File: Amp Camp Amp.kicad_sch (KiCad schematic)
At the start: 0 parts

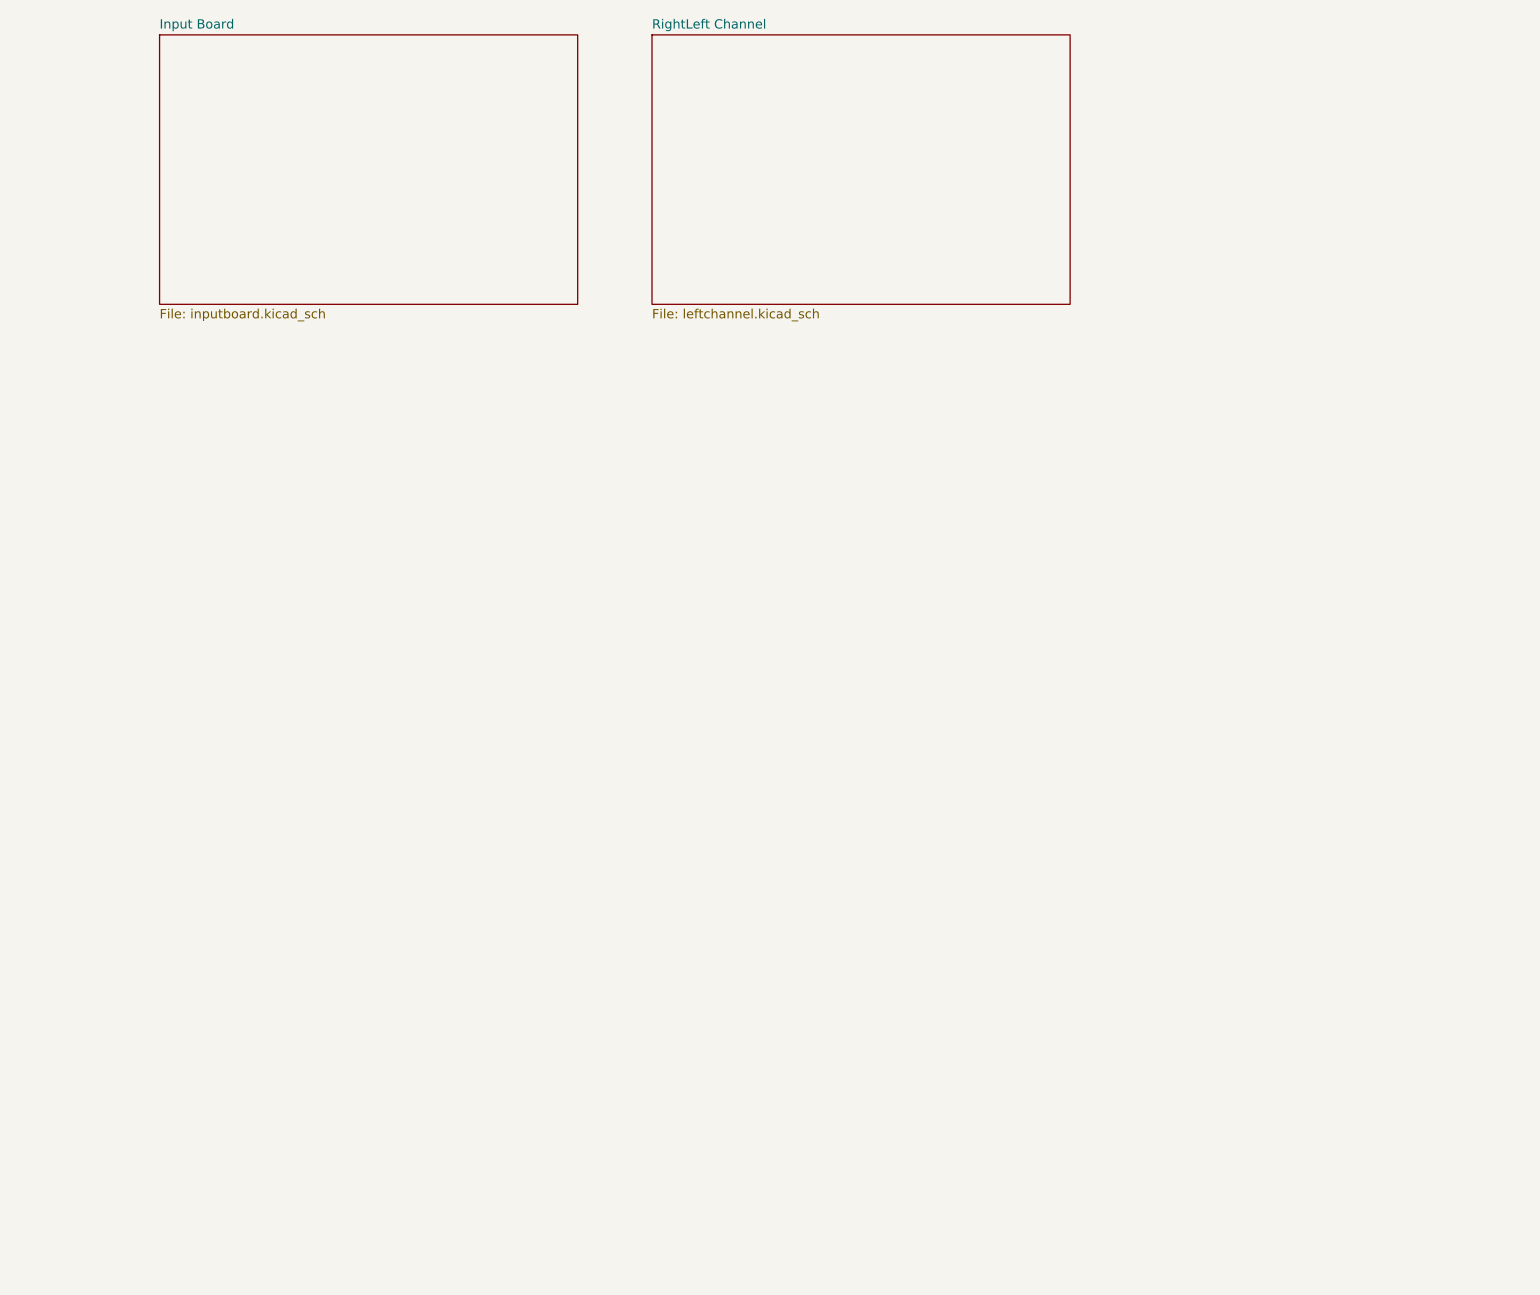
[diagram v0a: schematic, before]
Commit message: Updated the board to version 1.8
List of all differences between V1.6 and V1.8:

Rear switch is a 3 position DPDT instead of 2 position, necessitating a change in wiring
Rear panel is printed with a connection diagram
Chassis rails are improved using weld nuts and secured by bolts
Blade terminals are included for the front power switch
Longer wire
LED resistors have been changed from 10k to 33.2k to reduce LED brightness
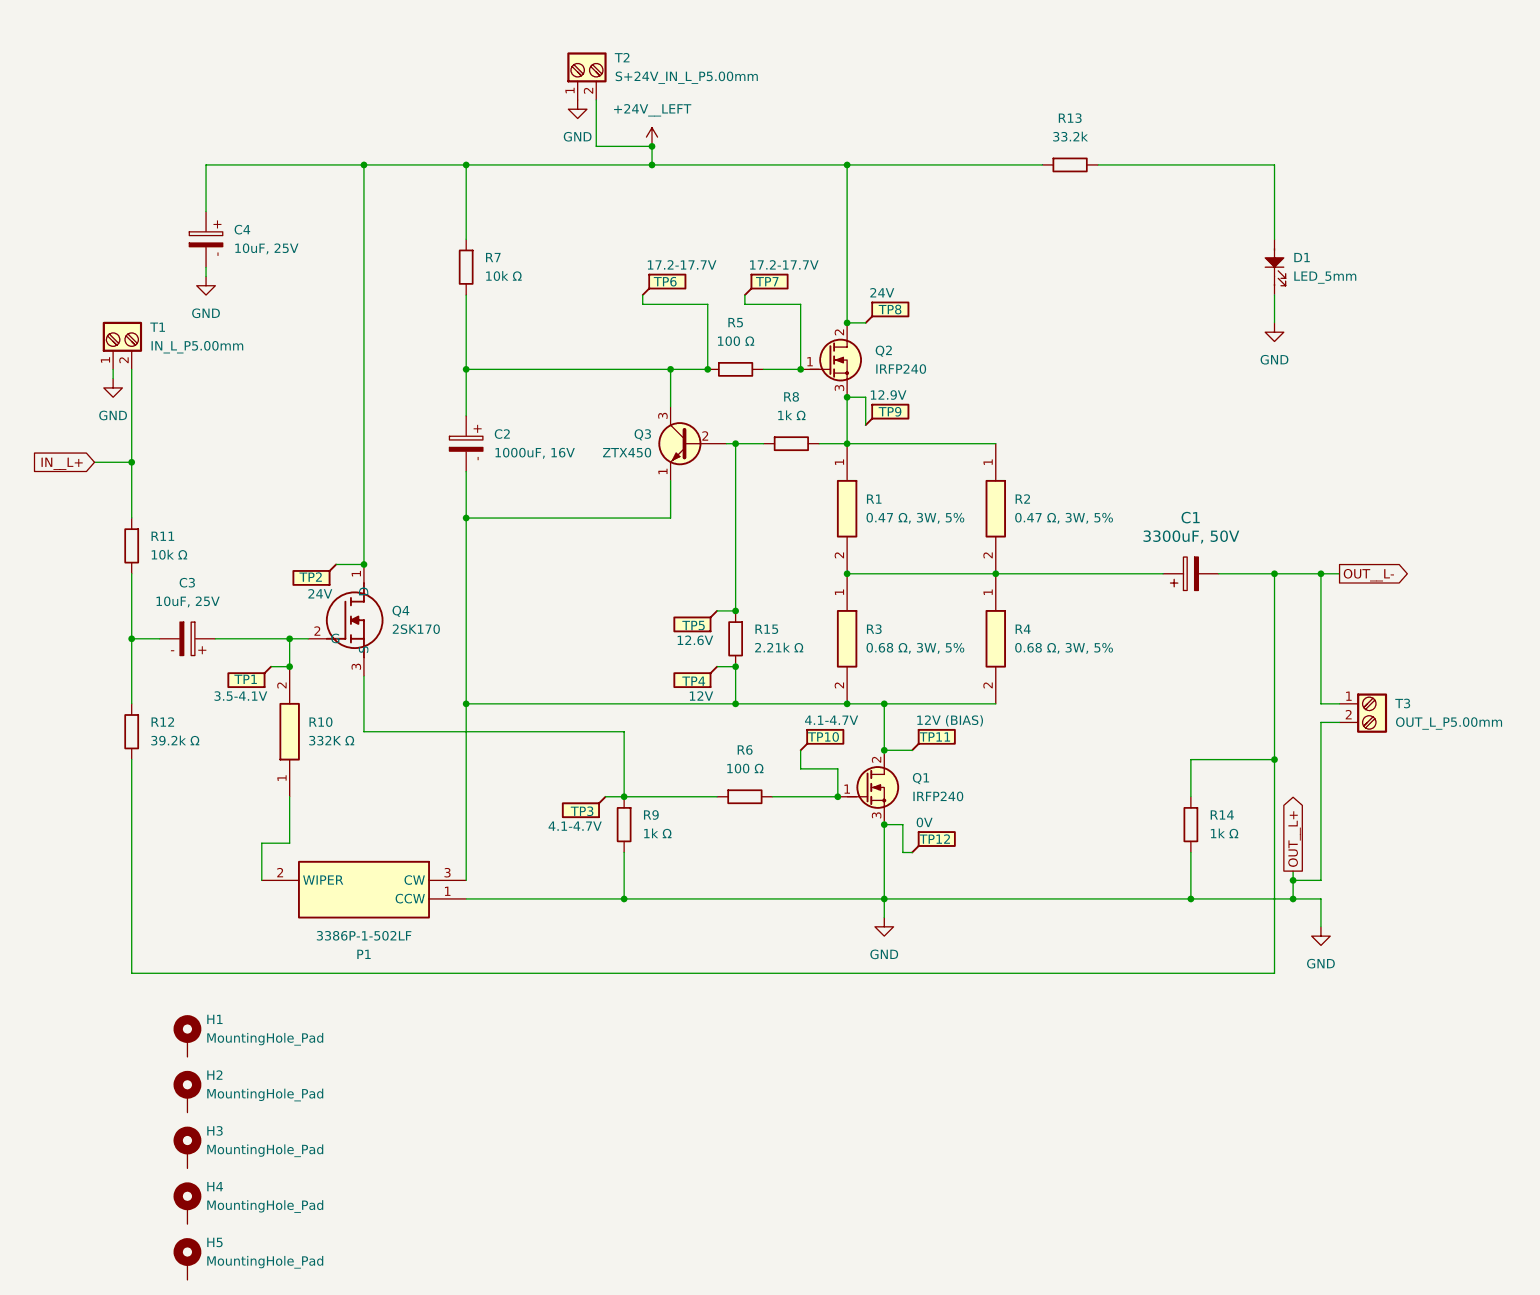
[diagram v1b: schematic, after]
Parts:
- added C1: 3300uF, 50V, PCM_Capacitor_THT_AKL:CP_Radial_D18.0mm_P7.50mm, symbol PCM_Capacitor_AKL:CP_Radial_D18.0mm_P7.50mm
- added C2: 1000uF, 16V, Capacitor_THT:CP_Radial_D10.0mm_P5.00mm, symbol PCM_SL_Capacitors:1000uF_16V
- added C3, C4: 10uF, 25V, Capacitor_THT:CP_Radial_D5.0mm_P2.00mm, symbol PCM_SL_Capacitors:10uF_25V
- added D1: LED_5mm, LED_THT:LED_D5.0mm, symbol PCM_SL_Devices:LED_5mm
- added H1, H2, H3, H4, H5: MountingHole_Pad, MountingHole:MountingHole_2.7mm_Pad, symbol Mechanical:MountingHole_Pad
- added P1: 3386P-1-502LF, Samacsys:3386P_1, symbol Samacsys:3386P-1-502LF
- added Q1, Q2: IRFP240, PCM_Package_TO_SOT_THT_AKL:TO-247-3_Vertical_GDS, symbol PCM_Transistor_MOSFET_AKL:IRFP240
- added Q3: ZTX450, PCM_Package_TO_SOT_THT_AKL:TO-92_Inline_Wide_EBC, symbol PCM_Transistor_BJT_AKL:ZTX450
- added Q4: 2SK170, Samacsys:2SK170, symbol Samacsys:2SK170
- added R1, R2: 0.47 Ω, 3W, 5%, Samacsys:RESAD3700W85L1500D550, symbol Samacsys:ERX-3SJR47V
- added R10: 332K Ω, Samacsys:RESAD1575W64L635D235, symbol Samacsys:RNF14FTD332K
- added R11, R7: 10k Ω, Resistor_THT:R_Axial_DIN0207_L6.3mm_D2.5mm_P10.16mm_Horizontal, symbol PCM_SL_Resistors:10k
- added R12: 39.2k Ω, Resistor_THT:R_Axial_DIN0207_L6.3mm_D2.5mm_P10.16mm_Horizontal, symbol PCM_SL_Resistors:39k
- added R13: 33.2k, Resistor_THT:R_Axial_DIN0207_L6.3mm_D2.5mm_P10.16mm_Horizontal, symbol PCM_SL_Resistors:33k
- added R14, R8, R9: 1k Ω, Resistor_THT:R_Axial_DIN0207_L6.3mm_D2.5mm_P10.16mm_Horizontal, symbol PCM_SL_Resistors:1k
- added R15: 2.21k Ω, Resistor_THT:R_Axial_DIN0207_L6.3mm_D2.5mm_P10.16mm_Horizontal, symbol PCM_SL_Resistors:2.2k
- added R3, R4: 0.68 Ω, 3W, 5%, Samacsys:RESAD3700W85L1500D550, symbol Samacsys:ERX-3SJR68A
- added R5, R6: 100 Ω, Resistor_THT:R_Axial_DIN0207_L6.3mm_D2.5mm_P10.16mm_Horizontal, symbol PCM_SL_Resistors:100ohm
- added T1: IN_L_P5.00mm, TerminalBlock_Phoenix:TerminalBlock_Phoenix_PT-1,5-2-5.0-H_1x02_P5.00mm_Horizontal, symbol PCM_SL_Screw_Terminal:Screw_Terminal_2_P5.00mm
- added T2: S+24V_IN_L_P5.00mm, TerminalBlock_Phoenix:TerminalBlock_Phoenix_PT-1,5-2-5.0-H_1x02_P5.00mm_Horizontal, symbol PCM_SL_Screw_Terminal:Screw_Terminal_2_P5.00mm
- added T3: OUT_L_P5.00mm, TerminalBlock_Phoenix:TerminalBlock_Phoenix_PT-1,5-2-5.0-H_1x02_P5.00mm_Horizontal, symbol PCM_SL_Screw_Terminal:Screw_Terminal_2_P5.00mm
- added TP1: 3.5-4.1V, TestPoint:TestPoint_Pad_D1.5mm, symbol Connector:TestPoint_Flag
- added TP10, TP3: 4.1-4.7V, TestPoint:TestPoint_Pad_D1.5mm, symbol Connector:TestPoint_Flag
- added TP11: 12V (BIAS), TestPoint:TestPoint_Pad_D1.5mm, symbol Connector:TestPoint_Flag
- added TP12: 0V, TestPoint:TestPoint_Pad_D1.5mm, symbol Connector:TestPoint_Flag
- added TP2, TP8: 24V, TestPoint:TestPoint_Pad_D1.5mm, symbol Connector:TestPoint_Flag
- added TP4: 12V, TestPoint:TestPoint_Pad_D1.5mm, symbol Connector:TestPoint_Flag
- added TP5: 12.6V, TestPoint:TestPoint_Pad_D1.5mm, symbol Connector:TestPoint_Flag
- added TP6, TP7: 17.2-17.7V, TestPoint:TestPoint_Pad_D1.5mm, symbol Connector:TestPoint_Flag
- added TP9: 12.9V, TestPoint:TestPoint_Pad_D1.5mm, symbol Connector:TestPoint_Flag
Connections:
- new net: D1.2, R13.2
- new net: C2.1, Q3.3 (C), R5.1, R7.2, TP6.1
- new net: Q2.1 (G), R5.2, TP7.1
- new net: Q4.3 (S), R6.1, R9.1, TP3.1
- new net: C2.2, P1.3 (CW), Q1.2 (D), Q3.1 (E), R15.2, R3.2, R4.2, TP11.1, TP4.1
- new net: Q3.2 (B), R15.1, R8.1, TP5.1
- new net: P1.2 (WIPER), R10.1
- new net: C1.1, R1.2, R2.2, R3.1, R4.1
- new net: C3.1, Q4.2 (G), R10.2, TP1.1
- new net: Q2.3 (S), R1.1, R2.1, R8.2, TP9.1
- new net: C3.2, R11.2, R12.1
- new net: Q1.1 (G), R6.2, TP10.1
- new net +24V__LEFT: C4.1, Q2.2 (D), Q4.1 (D), R13.1, R7.1, T2.2, TP2.1, TP8.1
- new net GND: C4.2, D1.1, P1.1 (CCW), Q1.3 (S), R14.2, R9.2, T1.1, T2.1, T3.2, TP12.1
- new net IN__L+: R11.1, T1.2
- new net OUT__L-: C1.2, R12.2, R14.1, T3.1
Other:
- removed sheet Input Board
- removed sheet RightLeft Channel

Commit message: Version change
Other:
- title: Amp Camp Amp v1.6 -> Amp Camp Amp v1.8
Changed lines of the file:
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@@
 	(paper "A4")
 	(title_block
-		(title "Amp Camp Amp v1.6")
+		(title "Amp Camp Amp v1.8")
 		(date "2024-11-19")
-		(rev "0")
+		(rev "1")
 		(company "Audiophi")
 	)
